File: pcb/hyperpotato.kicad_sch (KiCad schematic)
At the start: 46 parts, among them J1 Conn_01x02_Socket, J2 Conn_01x03_Pin, Q1 AO3401A, SW1 SW_Push_45deg, SW10 SW_Push_45deg, SW11 SW_Push_45deg, SW12 SW_Push_45deg, SW13 SW_Push_45deg, SW14 SW_SPDT, SW15 SW_Push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

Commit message: Route haptic driver
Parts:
- U1: footprint ssbb_parts:Xiao_nRF52840_AC_Reflow_reversible -> hyperpotato:Xiao_nRF52840_AC_Reflow_reversible
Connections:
- net COL0: now also U5.15 (QA); no longer U5.1 (QB)
- net COL1: now also U5.7 (QH); no longer U5.5 (QF)
- net COL2: now also U5.6 (QG); no longer U5.4 (QE)
- net COL3: now also U5.1 (QB); no longer U5.3 (QD)
- net LED1: now also U5.5 (QF); no longer U5.15 (QA)
- net LED2: now also U5.4 (QE); no longer U5.6 (QG)
- net LED3: now also U5.3 (QD); no longer U5.7 (QH)
- no-connect marks 10 -> 8
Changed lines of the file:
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@@
 	)
 	(no_connect
-		(at 81.28 232.41)
-	)
-	(no_connect
 		(at 55.88 166.37)
 	)
@@
 	)
 	(no_connect
-		(at 78.74 232.41)
-	)
-	(no_connect
 		(at 139.7 170.18)
 	)
@@
 		)
 	)
-	(global_label "TP_RST"
+	(global_label "COL3"
 		(shape input)
-		(at 139.7 160.02 0)
+		(at 204.47 172.72 0)
 		(fields_autoplaced yes)
 		(effects
@@
 		)
 		(property "Intersheetrefs" "${INTERSHEET_REFS}"
-			(at 149.3375 160.02 0)
+			(at 212.2933 172.72 0)
 			(effects
 				(font
@@
 		)
 	)
-	(global_label "TP_S3"
+	(global_label "LED2"
 		(shape input)
-		(at 133.35 191.77 0)
+		(at 204.47 180.34 0)
 		(fields_autoplaced yes)
 		(effects
@@
 		)
 		(property "Intersheetrefs" "${INTERSHEET_REFS}"
-			(at 141.9594 191.77 0)
+			(at 212.1118 180.34 0)
 			(effects
 				(font
@@
 		)
 	)
-	(global_label "IO_CS"
+	(global_label "TP_RST"
 		(shape input)
-		(at 181.61 182.88 180)
+		(at 139.7 160.02 0)
 		(fields_autoplaced yes)
 		(effects
@@
 				(size 1.27 1.27)
 			)
-			(justify right)
+			(justify left)
 		)
 		(property "Intersheetrefs" "${INTERSHEET_REFS}"
-			(at 173.3218 182.88 0)
+			(at 149.3375 160.02 0)
 			(effects
 				(font
 					(size 1.27 1.27)
 				)
-				(justify right)
+				(justify left)
 				(hide yes)
 			)
 		)
 	)
-	(global_label "COL2"
+	(global_label "TP_S3"
 		(shape input)
-		(at 204.47 180.34 0)
+		(at 133.35 191.77 0)
 		(fields_autoplaced yes)
 		(effects
@@
 		)
 		(property "Intersheetrefs" "${INTERSHEET_REFS}"
-			(at 212.2139 180.34 0)
+			(at 141.9594 191.77 0)
 			(effects
 				(font
@@
 		)
 	)
-	(global_label "SCK"
+	(global_label "IO_CS"
 		(shape input)
-		(at 99.06 255.27 0)
+		(at 181.61 182.88 180)
 		(fields_autoplaced yes)
 		(effects
@@
 				(size 1.27 1.27)
 			)
-			(justify left)
+			(justify right)
 		)
 		(property "Intersheetrefs" "${INTERSHEET_REFS}"
-			(at 105.7947 255.27 0)
+			(at 173.3218 182.88 0)
 			(effects
 				(font
 					(size 1.27 1.27)
 				)
-				(justify left)
+				(justify right)
 				(hide yes)
 			)
 		)
 	)
-	(global_label "COL4"
+	(global_label "SCK"
 		(shape input)
-		(at 204.47 175.26 0)
+		(at 99.06 255.27 0)
 		(fields_autoplaced yes)
 		(effects
@@
 		)
 		(property "Intersheetrefs" "${INTERSHEET_REFS}"
-			(at 212.2933 175.26 0)
+			(at 105.7947 255.27 0)
 			(effects
 				(font
@@
 		)
 	)
-	(global_label "LED1"
+	(global_label "COL2"
 		(shape input)
-		(at 204.47 170.18 0)
+		(at 204.47 185.42 0)
 		(fields_autoplaced yes)
 		(effects
@@
 		)
 		(property "Intersheetrefs" "${INTERSHEET_REFS}"
-			(at 212.1118 170.18 0)
+			(at 212.2139 185.42 0)
 			(effects
 				(font
@@
 		)
 	)
-	(global_label "COL0"
+	(global_label "SCL"
 		(shape input)
-		(at 204.47 172.72 0)
+		(at 43.18 173.99 180)
 		(fields_autoplaced yes)
 		(effects
@@
 				(size 1.27 1.27)
 			)
-			(justify left)
+			(justify right)
 		)
 		(property "Intersheetrefs" "${INTERSHEET_REFS}"
-			(at 212.2139 172.72 0)
+			(at 36.6872 173.99 0)
 			(effects
 				(font
 					(size 1.27 1.27)
 				)
-				(justify left)
+				(justify right)
 				(hide yes)
 			)
 		)
 	)
-	(global_label "LED3"
+	(global_label "COL1"
 		(shape input)
 		(at 204.47 187.96 0)
@@
 		)
 		(property "Intersheetrefs" "${INTERSHEET_REFS}"
-			(at 212.1118 187.96 0)
+			(at 212.2139 187.96 0)
 			(effects
 				(font
@@
 		)
 	)
-	(global_label "SCL"
-		(shape input)
-		(at 43.18 173.99 180)
-		(fields_autoplaced yes)
-		(effects
-			(font
-				(size 1.27 1.27)
-			)
-			(justify right)
-		)
-		(property "Intersheetrefs" "${INTERSHEET_REFS}"
-			(at 36.6872 173.99 0)
-			(effects
-				(font
-					(size 1.27 1.27)
-				)
-				(justify right)
-				(hide yes)
-			)
-		)
-	)
 	(global_label "COL2"
 		(shape input)
@@
 		)
 	)
-	(global_label "ROW0"
+	(global_label "COL4"
 		(shape input)
-		(at 26.67 44.45 180)
+		(at 204.47 175.26 0)
 		(fields_autoplaced yes)
 		(effects
@@
 				(size 1.27 1.27)
 			)
-			(justify right)
+			(justify left)
 		)
 		(property "Intersheetrefs" "${INTERSHEET_REFS}"
-			(at 18.4234 44.45 0)
+			(at 212.2933 175.26 0)
 			(effects
 				(font
 					(size 1.27 1.27)
 				)
-				(justify right)
+				(justify left)
 				(hide yes)
 			)
 		)
 	)
-	(global_label "TP_S1"
+	(global_label "LED3"
 		(shape input)
-		(at 111.76 162.56 180)
+		(at 204.47 177.8 0)
+		(fields_autoplaced yes)
+		(effects
+			(font
+				(size 1.27 1.27)
+			)
+			(justify left)
+		)
+		(property "Intersheetrefs" "${INTERSHEET_REFS}"
+			(at 212.1118 177.8 0)
+			(effects
+				(font
+					(size 1.27 1.27)
+				)
+				(justify left)
+				(hide yes)
+			)
+		)
+	)
+	(global_label "ROW0"
+		(shape input)
+		(at 26.67 44.45 180)
 		(fields_autoplaced yes)
 		(effects
@@
 		)
 		(property "Intersheetrefs" "${INTERSHEET_REFS}"
-			(at 103.1506 162.56 0)
+			(at 18.4234 44.45 0)
 			(effects
 				(font
@@
 		)
 	)
-	(global_label "MOSI"
+	(global_label "TP_S1"
 		(shape input)
-		(at 181.61 170.18 180)
+		(at 111.76 162.56 180)
 		(fields_autoplaced yes)
 		(effects
@@
 		)
 		(property "Intersheetrefs" "${INTERSHEET_REFS}"
-			(at 174.108 170.18 0)
+			(at 103.1506 162.56 0)
 			(effects
 				(font
@@
 		)
 	)
-	(global_label "COL4"
+	(global_label "MOSI"
 		(shape input)
-		(at 81.28 27.94 90)
+		(at 181.61 170.18 180)
 		(fields_autoplaced yes)
 		(effects
@@
 				(size 1.27 1.27)
 			)
-			(justify left)
+			(justify right)
 		)
 		(property "Intersheetrefs" "${INTERSHEET_REFS}"
-			(at 81.28 20.1167 90)
+			(at 174.108 170.18 0)
 			(effects
 				(font
 					(size 1.27 1.27)
 				)
-				(justify left)
+				(justify right)
 				(hide yes)
 			)
 		)
 	)
-	(global_label "COL1"
+	(global_label "COL4"
 		(shape input)
-		(at 204.47 182.88 0)
+		(at 81.28 27.94 90)
 		(fields_autoplaced yes)
 		(effects
@@
 		)
 		(property "Intersheetrefs" "${INTERSHEET_REFS}"
-			(at 212.2139 182.88 0)
+			(at 81.28 20.1167 90)
 			(effects
 				(font
@@
 		)
 	)
+	(global_label "LED1"
+		(shape input)
+		(at 204.47 182.88 0)
+		(fields_autoplaced yes)
+		(effects
+			(font
+				(size 1.27 1.27)
+			)
+			(justify left)
+		)
+		(property "Intersheetrefs" "${INTERSHEET_REFS}"
+			(at 212.1118 182.88 0)
+			(effects
+				(font
+					(size 1.27 1.27)
+				)
+				(justify left)
+				(hide yes)
+			)
+		)
+	)
 	(global_label "COL0"
 		(shape input)
@@
 		)
 	)
-	(global_label "LED2"
+	(global_label "COL0"
 		(shape input)
-		(at 204.47 185.42 0)
+		(at 204.47 170.18 0)
 		(fields_autoplaced yes)
 		(effects
@@
 		)
 		(property "Intersheetrefs" "${INTERSHEET_REFS}"
-			(at 212.1118 185.42 0)
+			(at 212.2139 170.18 0)
 			(effects
 				(font
@@
 		)
 	)
-	(global_label "COL3"
-		(shape input)
-		(at 204.47 177.8 0)
-		(fields_autoplaced yes)
-		(effects
-			(font
-				(size 1.27 1.27)
-			)
-			(justify left)
-		)
-		(property "Intersheetrefs" "${INTERSHEET_REFS}"
-			(at 212.2933 177.8 0)
-			(effects
-				(font
-					(size 1.27 1.27)
-				)
-				(justify left)
-				(hide yes)
-			)
-		)
-	)
 	(global_label "SDA"
 		(shape input)
@@
 			)
 		)
-		(property "Footprint" "ssbb_parts:Xiao_nRF52840_AC_Reflow_reversible"
+		(property "Footprint" "hyperpotato:Xiao_nRF52840_AC_Reflow_reversible"
 			(at 81.28 287.02 0)
 			(effects

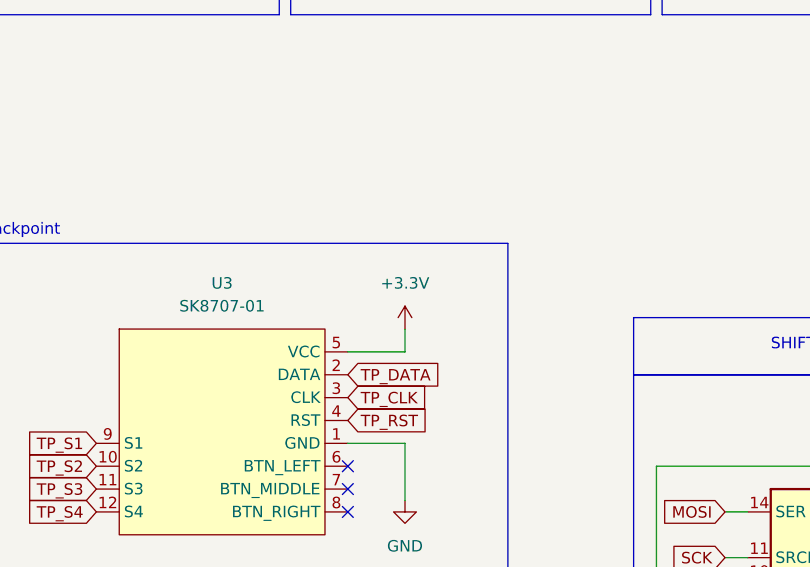
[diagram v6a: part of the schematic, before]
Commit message: Almost routed, changing 595 package
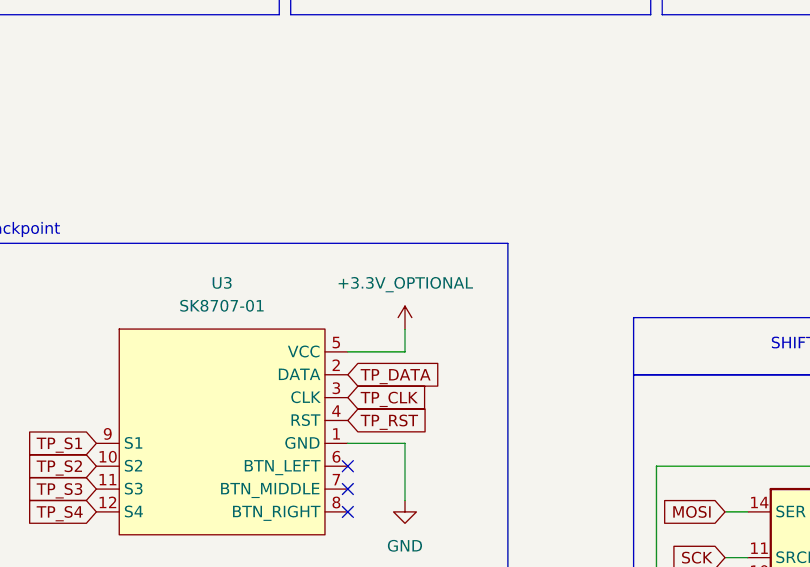
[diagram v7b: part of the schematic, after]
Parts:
- Q1: footprint Package_TO_SOT_SMD:SOT-23 -> hyperpotato:SOT-23_reversible
- SW1, SW10, SW11, SW12, SW13, SW2, SW3, SW4, SW5, SW6, SW7, SW8, SW9: footprint ssbb_parts:SW_Choc_Mini_reversible_1u -> hyperpotato:SW_Choc_Mini_reversible_1u
- U1: footprint hyperpotato:Xiao_nRF52840_AC_Reflow_reversible -> hyperpotato:XIAO-nRF52840-Sense-14P-2.54-21X17.8MM_1
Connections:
- net +3.3V: no longer U3.5 (VCC)
- net +3.3V_OPTIONAL: now also U3.5 (VCC)
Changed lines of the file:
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@@
 			)
 		)
-		(property "Footprint" "ssbb_parts:SW_Choc_Mini_reversible_1u"
+		(property "Footprint" "hyperpotato:SW_Choc_Mini_reversible_1u"
 			(at 45.72 63.5 0)
 			(effects
@@
 			)
 		)
-		(property "Footprint" "ssbb_parts:SW_Choc_Mini_reversible_1u"
+		(property "Footprint" "hyperpotato:SW_Choc_Mini_reversible_1u"
 			(at 71.12 63.5 0)
 			(effects
@@
 			)
 		)
-		(property "Footprint" "ssbb_parts:SW_Choc_Mini_reversible_1u"
+		(property "Footprint" "hyperpotato:SW_Choc_Mini_reversible_1u"
 			(at 71.12 36.83 0)
 			(effects
@@
 			)
 		)
-		(property "Footprint" "hyperpotato:Xiao_nRF52840_AC_Reflow_reversible"
+		(property "Footprint" "hyperpotato:XIAO-nRF52840-Sense-14P-2.54-21X17.8MM_1"
 			(at 81.28 287.02 0)
 			(effects
@@
 			)
 		)
-		(property "Footprint" "ssbb_parts:SW_Choc_Mini_reversible_1u"
+		(property "Footprint" "hyperpotato:SW_Choc_Mini_reversible_1u"
 			(at 45.72 36.83 0)
 			(effects
@@
 			)
 		)
-		(property "Footprint" "ssbb_parts:SW_Choc_Mini_reversible_1u"
+		(property "Footprint" "hyperpotato:SW_Choc_Mini_reversible_1u"
 			(at 45.72 49.53 0)
 			(effects
@@
 			)
 		)
-		(property "Footprint" "ssbb_parts:SW_Choc_Mini_reversible_1u"
+		(property "Footprint" "hyperpotato:SW_Choc_Mini_reversible_1u"
 			(at 33.02 49.53 0)
 			(effects
@@
 			)
 		)
-		(property "Footprint" "ssbb_parts:SW_Choc_Mini_reversible_1u"
+		(property "Footprint" "hyperpotato:SW_Choc_Mini_reversible_1u"
 			(at 71.12 49.53 0)
 			(effects
@@
 			)
 		)
-		(property "Footprint" "ssbb_parts:SW_Choc_Mini_reversible_1u"
+		(property "Footprint" "hyperpotato:SW_Choc_Mini_reversible_1u"
 			(at 58.42 49.53 0)
 			(effects
@@
 			)
 		)
-		(property "Footprint" "Package_TO_SOT_SMD:SOT-23"
+		(property "Footprint" "hyperpotato:SOT-23_reversible"
 			(at 108.585 109.22 0)
 			(effects
@@
 	)
 	(symbol
-		(lib_id "power:+3.3V")
-		(at 146.05 149.86 0)
-		(unit 1)
-		(exclude_from_sim no)
-		(in_bom yes)
-		(on_board yes)
-		(dnp no)
-		(fields_autoplaced yes)
-		(property "Reference" "#PWR06"
-			(at 146.05 153.67 0)
-			(effects
-				(font
-					(size 1.27 1.27)
-				)
-				(hide yes)
-			)
-		)
-		(property "Value" "+3.3V"
-			(at 146.05 144.78 0)
-			(effects
-				(font
-					(size 1.27 1.27)
-				)
-			)
-		)
-		(property "Footprint" ""
-			(at 146.05 149.86 0)
-			(effects
-				(font
-					(size 1.27 1.27)
-				)
-				(hide yes)
-			)
-		)
-		(property "Datasheet" ""
-			(at 146.05 149.86 0)
-			(effects
-				(font
-					(size 1.27 1.27)
-				)
-				(hide yes)
-			)
-		)
-		(property "Description" "Power symbol creates a global label with name \"+3.3V\""
-			(at 146.05 149.86 0)
-			(effects
-				(font
-					(size 1.27 1.27)
-				)
-				(hide yes)
-			)
-		)
-		(pin "1"
-		)
-		(instances
-			(project ""
-				(path "/19b5f7b9-14b9-4ffe-8621-f024a09d5ec4"
-					(reference "#PWR06")
-					(unit 1)
-				)
-			)
-		)
-	)
-	(symbol
 		(lib_name "SW_Push_45deg_3")
 		(lib_id "Switch:SW_Push_45deg")
@@
 			)
 		)
-		(property "Footprint" "ssbb_parts:SW_Choc_Mini_reversible_1u"
+		(property "Footprint" "hyperpotato:SW_Choc_Mini_reversible_1u"
 			(at 58.42 36.83 0)
 			(effects
@@
 			)
 		)
-		(property "Footprint" "ssbb_parts:SW_Choc_Mini_reversible_1u"
+		(property "Footprint" "hyperpotato:SW_Choc_Mini_reversible_1u"
 			(at 83.82 49.53 0)
 			(effects
@@
 			)
 		)
-		(property "Footprint" "ssbb_parts:SW_Choc_Mini_reversible_1u"
+		(property "Footprint" "hyperpotato:SW_Choc_Mini_reversible_1u"
 			(at 83.82 36.83 0)
 			(effects
@@
 			)
 		)
-		(property "Footprint" "ssbb_parts:SW_Choc_Mini_reversible_1u"
+		(property "Footprint" "hyperpotato:SW_Choc_Mini_reversible_1u"
 			(at 58.42 63.5 0)
 			(effects
@@
 	)
 	(symbol
+		(lib_id "ssbb_parts:+3.3V_OPTIONAL")
+		(at 146.05 149.86 0)
+		(unit 1)
+		(exclude_from_sim no)
+		(in_bom yes)
+		(on_board yes)
+		(dnp no)
+		(fields_autoplaced yes)
+		(property "Reference" "#PWR06"
+			(at 146.05 153.67 0)
+			(effects
+				(font
+					(size 1.27 1.27)
+				)
+				(hide yes)
+			)
+		)
+		(property "Value" "+3.3V_OPTIONAL"
+			(at 146.05 144.78 0)
+			(effects
+				(font
+					(size 1.27 1.27)
+				)
+			)
+		)
+		(property "Footprint" ""
+			(at 146.05 149.86 0)
+			(effects
+				(font
+					(size 1.27 1.27)
+				)
+				(hide yes)
+			)
+		)
+		(property "Datasheet" ""
+			(at 146.05 149.86 0)
+			(effects
+				(font
+					(size 1.27 1.27)
+				)
+				(hide yes)
+			)
+		)
+		(property "Description" "Power symbol creates a global label with name \"+3.3V_OPTIONAL\""
+			(at 146.05 149.86 0)
+			(effects
+				(font
+					(size 1.27 1.27)
+				)
+				(hide yes)
+			)
+		)
+		(pin "1"
+		)
+		(instances
+			(project ""
+				(path "/19b5f7b9-14b9-4ffe-8621-f024a09d5ec4"
+					(reference "#PWR06")
+					(unit 1)
+				)
+			)
+		)
+	)
+	(symbol
 		(lib_id "Switch:SW_SPDT")
 		(at 149.86 95.25 0)
@@
 			)
 		)
-		(property "Footprint" "ssbb_parts:SW_Choc_Mini_reversible_1u"
+		(property "Footprint" "hyperpotato:SW_Choc_Mini_reversible_1u"
 			(at 83.82 63.5 0)
 			(effects

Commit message: Good progress on routing
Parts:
- U5: footprint ssbb_parts_reversible:SOIC-16_3.9x9.9mm_P1.27mm_reversible -> ssbb_parts_reversible:TSSOP-16_4.4x5mm_P0.65mm_reversible
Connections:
- net MOSI: now also U1.13 (P1.13-D8-LF); no longer U1.11 (P1.15-D10-LF)
- net POWER_CUTOFF: now also U1.14 (P1.12-D7-LF); no longer U1.7 (P1.11-D6-LF)
- net SCK: now also U1.11 (P1.15-D10-LF); no longer U1.13 (P1.13-D8-LF)
- net TP_CLK: now also U1.6 (P0.05-D5); no longer U1.5 (P0.04-D4)
- net TP_DATA: now also U1.5 (P0.04-D4); no longer U1.6 (P0.05-D5)
- net TP_RST: now also U1.7 (P1.11-D6-LF); no longer U1.14 (P1.12-D7-LF)
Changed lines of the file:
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@@
 		)
 	)
-	(global_label "IO_CS"
+	(global_label "SCL"
 		(shape input)
-		(at 181.61 182.88 180)
+		(at 86.36 275.59 270)
 		(fields_autoplaced yes)
 		(effects
@@
 		)
 		(property "Intersheetrefs" "${INTERSHEET_REFS}"
-			(at 173.3218 182.88 0)
+			(at 86.36 282.0828 90)
 			(effects
 				(font
@@
 		)
 	)
-	(global_label "SCK"
+	(global_label "IO_CS"
 		(shape input)
-		(at 99.06 255.27 0)
+		(at 181.61 182.88 180)
 		(fields_autoplaced yes)
 		(effects
@@
 				(size 1.27 1.27)
 			)
-			(justify left)
+			(justify right)
 		)
 		(property "Intersheetrefs" "${INTERSHEET_REFS}"
-			(at 105.7947 255.27 0)
+			(at 173.3218 182.88 0)
 			(effects
 				(font
 					(size 1.27 1.27)
 				)
-				(justify left)
+				(justify right)
 				(hide yes)
 			)
@@
 		)
 	)
+	(global_label "SCK"
+		(shape input)
+		(at 99.06 250.19 0)
+		(fields_autoplaced yes)
+		(effects
+			(font
+				(size 1.27 1.27)
+			)
+			(justify left)
+		)
+		(property "Intersheetrefs" "${INTERSHEET_REFS}"
+			(at 105.7947 250.19 0)
+			(effects
+				(font
+					(size 1.27 1.27)
+				)
+				(justify left)
+				(hide yes)
+			)
+		)
+	)
 	(global_label "RESET"
 		(shape input)
@@
 		)
 	)
-	(global_label "POWER_CUTOFF"
+	(global_label "TP_CLK"
 		(shape input)
-		(at 63.5 257.81 180)
+		(at 63.5 255.27 180)
 		(fields_autoplaced yes)
 		(effects
@@
 		)
 		(property "Intersheetrefs" "${INTERSHEET_REFS}"
-			(at 46.0005 257.81 0)
+			(at 53.7415 255.27 0)
 			(effects
 				(font
@@
 		)
 	)
-	(global_label "MOSI"
-		(shape input)
-		(at 99.06 250.19 0)
-		(fields_autoplaced yes)
-		(effects
-			(font
-				(size 1.27 1.27)
-			)
-			(justify left)
-		)
-		(property "Intersheetrefs" "${INTERSHEET_REFS}"
-			(at 106.6414 250.19 0)
-			(effects
-				(font
-					(size 1.27 1.27)
-				)
-				(justify left)
-				(hide yes)
-			)
-		)
-	)
-	(global_label "TP_RST"
+	(global_label "RESET"
 		(shape input)
-		(at 99.06 257.81 0)
+		(at 83.82 232.41 90)
 		(fields_autoplaced yes)
 		(effects
@@
 		)
 		(property "Intersheetrefs" "${INTERSHEET_REFS}"
-			(at 108.6975 257.81 0)
+			(at 83.82 223.6797 90)
 			(effects
 				(font
@@
 		)
 	)
-	(global_label "RESET"
+	(global_label "POWER_CUTOFF"
 		(shape input)
-		(at 83.82 232.41 90)
+		(at 110.49 86.36 0)
 		(fields_autoplaced yes)
 		(effects
@@
 		)
 		(property "Intersheetrefs" "${INTERSHEET_REFS}"
-			(at 83.82 223.6797 90)
+			(at 127.9895 86.36 0)
 			(effects
 				(font
@@
 		)
 	)
-	(global_label "POWER_CUTOFF"
+	(global_label "COL4"
 		(shape input)
-		(at 110.49 86.36 0)
+		(at 204.47 175.26 0)
 		(fields_autoplaced yes)
 		(effects
@@
 		)
 		(property "Intersheetrefs" "${INTERSHEET_REFS}"
-			(at 127.9895 86.36 0)
+			(at 212.2933 175.26 0)
 			(effects
 				(font
@@
 		)
 	)
-	(global_label "COL4"
+	(global_label "LED3"
 		(shape input)
-		(at 204.47 175.26 0)
+		(at 204.47 177.8 0)
 		(fields_autoplaced yes)
 		(effects
@@
 		)
 		(property "Intersheetrefs" "${INTERSHEET_REFS}"
-			(at 212.2933 175.26 0)
+			(at 212.1118 177.8 0)
 			(effects
 				(font
@@
 		)
 	)
-	(global_label "LED3"
+	(global_label "MOSI"
 		(shape input)
-		(at 204.47 177.8 0)
+		(at 99.06 255.27 0)
 		(fields_autoplaced yes)
 		(effects
@@
 		)
 		(property "Intersheetrefs" "${INTERSHEET_REFS}"
-			(at 212.1118 177.8 0)
+			(at 106.6414 255.27 0)
 			(effects
 				(font
@@
 		)
 	)
-	(global_label "COL4"
+	(global_label "POWER_CUTOFF"
 		(shape input)
-		(at 81.28 27.94 90)
+		(at 99.06 257.81 0)
 		(fields_autoplaced yes)
 		(effects
@@
 		)
 		(property "Intersheetrefs" "${INTERSHEET_REFS}"
-			(at 81.28 20.1167 90)
+			(at 112.4833 257.81 0)
 			(effects
 				(font
@@
 		)
 	)
-	(global_label "SCL"
+	(global_label "TP_RST"
 		(shape input)
-		(at 86.36 275.59 270)
+		(at 63.5 257.81 180)
 		(fields_autoplaced yes)
 		(effects
@@
 		)
 		(property "Intersheetrefs" "${INTERSHEET_REFS}"
-			(at 86.36 282.0828 90)
+			(at 55.407 257.81 0)
 			(effects
 				(font
@@
 		)
 	)
-	(global_label "TP_CLK"
+	(global_label "COL4"
 		(shape input)
-		(at 139.7 157.48 0)
+		(at 81.28 27.94 90)
 		(fields_autoplaced yes)
 		(effects
@@
 		)
 		(property "Intersheetrefs" "${INTERSHEET_REFS}"
-			(at 149.4585 157.48 0)
+			(at 81.28 20.1167 90)
 			(effects
 				(font
@@
 		)
 	)
-	(global_label "TP_DATA"
+	(global_label "SDA"
 		(shape input)
-		(at 63.5 255.27 180)
+		(at 88.9 275.59 270)
 		(fields_autoplaced yes)
 		(effects
@@
 		)
 		(property "Intersheetrefs" "${INTERSHEET_REFS}"
-			(at 52.8948 255.27 0)
+			(at 88.9 282.1433 90)
 			(effects
 				(font
@@
 		)
 	)
+	(global_label "TP_CLK"
+		(shape input)
+		(at 139.7 157.48 0)
+		(fields_autoplaced yes)
+		(effects
+			(font
+				(size 1.27 1.27)
+			)
+			(justify left)
+		)
+		(property "Intersheetrefs" "${INTERSHEET_REFS}"
+			(at 149.4585 157.48 0)
+			(effects
+				(font
+					(size 1.27 1.27)
+				)
+				(justify left)
+				(hide yes)
+			)
+		)
+	)
 	(global_label "TP_S1"
 		(shape input)
@@
 		)
 	)
-	(global_label "TP_CLK"
-		(shape input)
-		(at 63.5 252.73 180)
-		(fields_autoplaced yes)
-		(effects
-			(font
-				(size 1.27 1.27)
-			)
-			(justify right)
-		)
-		(property "Intersheetrefs" "${INTERSHEET_REFS}"
-			(at 53.7415 252.73 0)
-			(effects
-				(font
-					(size 1.27 1.27)
-				)
-				(justify right)
-				(hide yes)
-			)
-		)
-	)
 	(global_label "LED1"
 		(shape input)
@@
 		)
 	)
-	(global_label "SDA"
+	(global_label "TP_DATA"
 		(shape input)
-		(at 88.9 275.59 270)
+		(at 63.5 252.73 180)
 		(fields_autoplaced yes)
 		(effects
@@
 		)
 		(property "Intersheetrefs" "${INTERSHEET_REFS}"
-			(at 88.9 282.1433 90)
+			(at 52.8948 252.73 0)
 			(effects
 				(font
@@
 			)
 		)
-		(property "Footprint" "ssbb_parts_reversible:SOIC-16_3.9x9.9mm_P1.27mm_reversible"
+		(property "Footprint" "ssbb_parts_reversible:TSSOP-16_4.4x5mm_P0.65mm_reversible"
 			(at 194.31 180.34 0)
 			(effects
